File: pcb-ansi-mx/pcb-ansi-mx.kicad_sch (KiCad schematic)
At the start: 209 parts, among them J1 USB_C_Receptacle_USB2.0, J3 Conn_01x05, SW1 SW_Push, SW2 SW_Push, U1 XC6206PxxxMR, U2 SRV05-4, U3 RP2040, U4 W25Q128JVS, Y1 Crystal_GND24

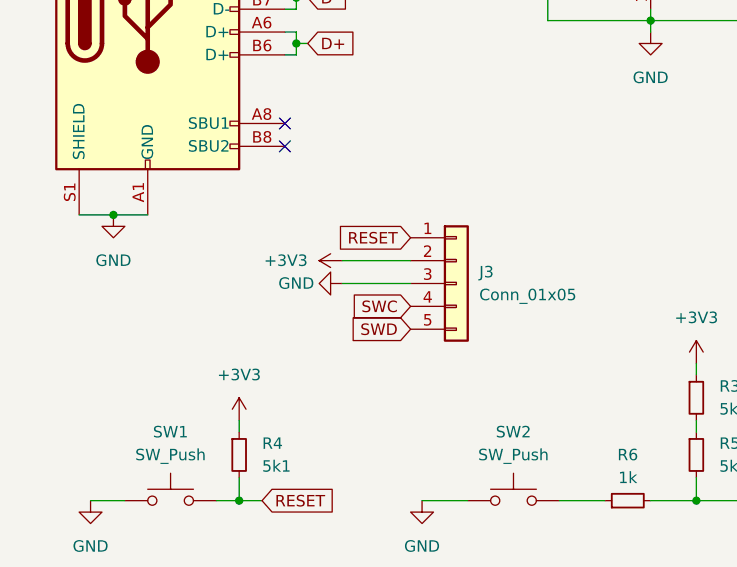
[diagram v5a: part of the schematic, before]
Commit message: feat: route everything but encoder and matrix
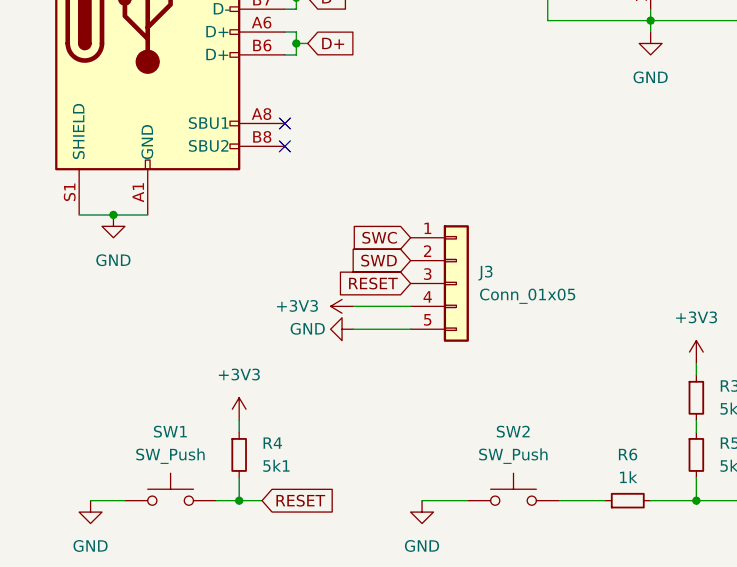
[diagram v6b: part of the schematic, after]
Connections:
- net +3V3: now also J3.4 (Pin_4); no longer J3.2 (Pin_2)
- net GND: now also J3.5 (Pin_5); no longer J3.3 (Pin_3)
- net RESET: now also J3.3 (Pin_3); no longer J3.1 (Pin_1)
- net SWC: now also J3.1 (Pin_1); no longer J3.4 (Pin_4)
- net SWD: now also J3.2 (Pin_2); no longer J3.5 (Pin_5)
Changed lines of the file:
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@@
     (stroke (width 0) (type default))
   )
+  (wire (pts (xy 53.34 73.66) (xy 59.69 73.66))
+    (stroke (width 0) (type default))
+  )
   (wire (pts (xy 166.37 195.58) (xy 166.37 214.63))
     (stroke (width 0) (type default))
@@
     (stroke (width 0) (type default))
   )
-  (wire (pts (xy 52.07 68.58) (xy 59.69 68.58))
-    (stroke (width 0) (type default))
-  )
   (wire (pts (xy 33.02 118.11) (xy 43.18 118.11))
     (stroke (width 0) (type default))
@@
     (stroke (width 0) (type default))
   )
+  (wire (pts (xy 53.34 71.12) (xy 59.69 71.12))
+    (stroke (width 0) (type default))
+  )
   (wire (pts (xy 260.35 167.64) (xy 273.05 167.64))
     (stroke (width 0) (type default))
@@
     (stroke (width 0) (type default))
   )
-  (wire (pts (xy 52.07 66.04) (xy 59.69 66.04))
-    (stroke (width 0) (type default))
-  )
   (wire (pts (xy 45.72 38.1) (xy 46.99 38.1))
     (stroke (width 0) (type default))
@@
     )
   )
-  (global_label "SWD" (shape input) (at 59.69 73.66 180) (fields_autoplaced)
+  (global_label "SWD" (shape input) (at 59.69 66.04 180) (fields_autoplaced)
     (effects (font (size 1.27 1.27)) (justify right))
-    (property "Intersheetrefs" "${INTERSHEET_REFS}" (at 52.7739 73.66 0)
+    (property "Intersheetrefs" "${INTERSHEET_REFS}" (at 52.7739 66.04 0)
       (effects (font (size 1.27 1.27)) (justify right) hide)
     )
@@
     )
   )
-  (global_label "SWC" (shape input) (at 59.69 71.12 180) (fields_autoplaced)
+  (global_label "SWC" (shape input) (at 59.69 63.5 180) (fields_autoplaced)
     (effects (font (size 1.27 1.27)) (justify right))
-    (property "Intersheetrefs" "${INTERSHEET_REFS}" (at 52.7739 71.12 0)
+    (property "Intersheetrefs" "${INTERSHEET_REFS}" (at 52.7739 63.5 0)
       (effects (font (size 1.27 1.27)) (justify right) hide)
     )
@@
     )
   )
-  (global_label "RESET" (shape input) (at 59.69 63.5 180) (fields_autoplaced)
+  (global_label "RESET" (shape input) (at 59.69 68.58 180) (fields_autoplaced)
     (effects (font (size 1.27 1.27)) (justify right))
-    (property "Intersheetrefs" "${INTERSHEET_REFS}" (at 50.9597 63.5 0)
+    (property "Intersheetrefs" "${INTERSHEET_REFS}" (at 50.9597 68.58 0)
       (effects (font (size 1.27 1.27)) (justify right) hide)
     )
@@
     )
   )
-  (symbol (lib_id "power:+3V3") (at 52.07 66.04 90) (unit 1)
+  (symbol (lib_id "power:+3V3") (at 53.34 71.12 90) (unit 1)
     (in_bom yes) (on_board yes) (dnp no) (fields_autoplaced)
-    (property "Reference" "#PWR010" (at 55.88 66.04 0)
+    (property "Reference" "#PWR010" (at 57.15 71.12 0)
       (effects (font (size 1.27 1.27)) hide)
     )
-    (property "Value" "+3V3" (at 48.26 66.04 90)
+    (property "Value" "+3V3" (at 49.53 71.12 90)
       (effects (font (size 1.27 1.27)) (justify left))
     )
-    (property "Footprint" "" (at 52.07 66.04 0)
+    (property "Footprint" "" (at 53.34 71.12 0)
       (effects (font (size 1.27 1.27)) hide)
     )
-    (property "Datasheet" "" (at 52.07 66.04 0)
+    (property "Datasheet" "" (at 53.34 71.12 0)
       (effects (font (size 1.27 1.27)) hide)
     )
@@
     )
   )
-  (symbol (lib_id "power:GND") (at 52.07 68.58 270) (unit 1)
+  (symbol (lib_id "power:GND") (at 53.34 73.66 270) (unit 1)
     (in_bom yes) (on_board yes) (dnp no)
-    (property "Reference" "#PWR012" (at 45.72 68.58 0)
+    (property "Reference" "#PWR012" (at 46.99 73.66 0)
       (effects (font (size 1.27 1.27)) hide)
     )
-    (property "Value" "GND" (at 46.99 68.58 90)
+    (property "Value" "GND" (at 48.26 73.66 90)
       (effects (font (size 1.27 1.27)))
     )
-    (property "Footprint" "" (at 52.07 68.58 0)
+    (property "Footprint" "" (at 53.34 73.66 0)
       (effects (font (size 1.27 1.27)) hide)
     )
-    (property "Datasheet" "" (at 52.07 68.58 0)
+    (property "Datasheet" "" (at 53.34 73.66 0)
       (effects (font (size 1.27 1.27)) hide)
     )
